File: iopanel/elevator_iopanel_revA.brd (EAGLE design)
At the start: 133.1 x 99.1 mm, 48 parts, among them U2 TLC6C598-Q1, U3 TLC6C598-Q1, U4 SN74HC165DR, U6 TLC6C598-Q1, X3 MSTBA2

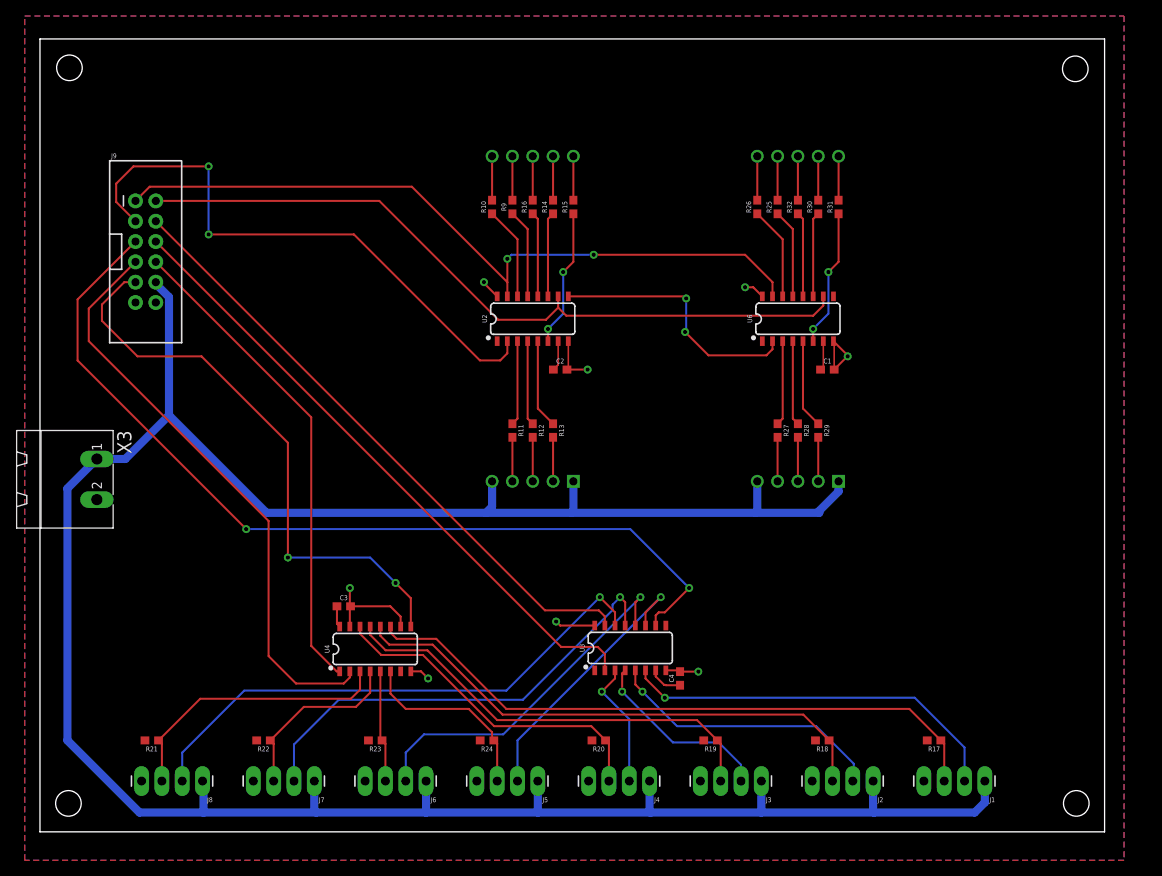
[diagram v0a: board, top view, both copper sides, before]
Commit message: Added LEDs for power rails, silkscreen. sent to fab
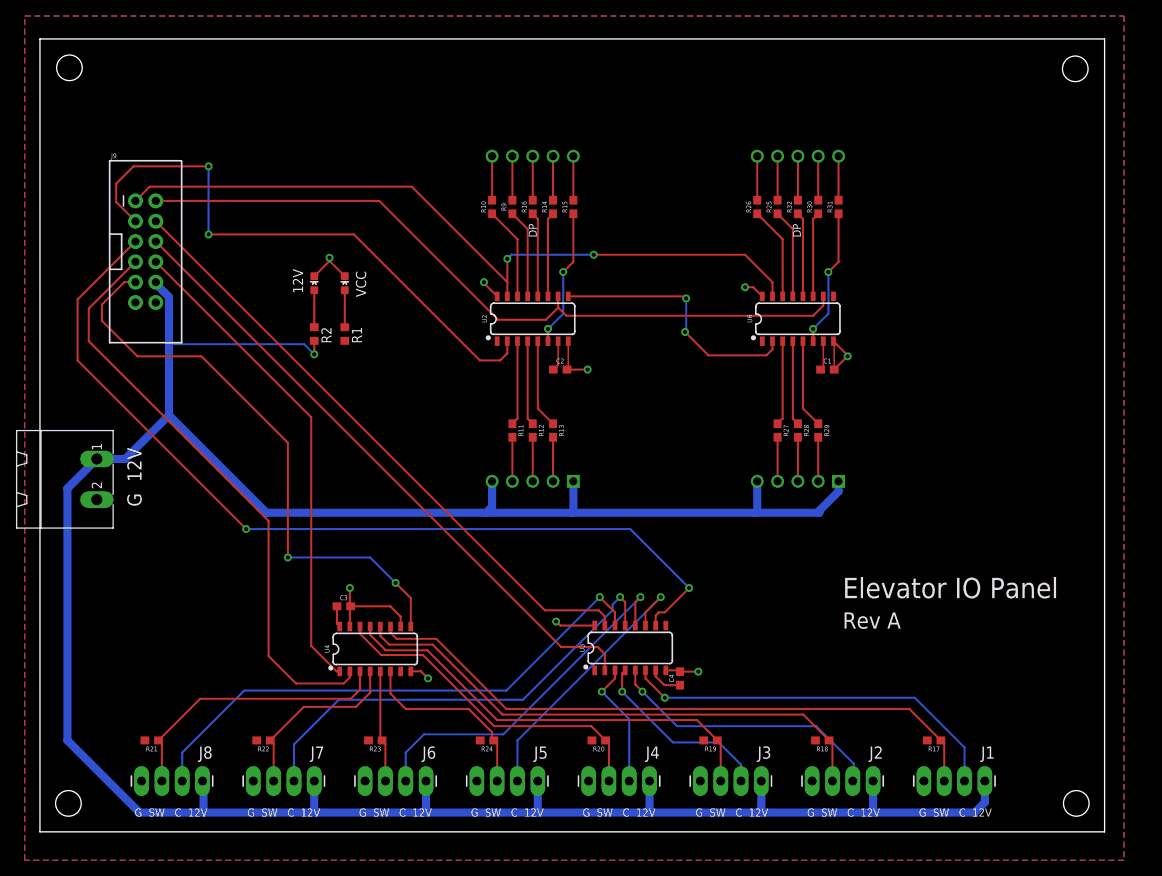
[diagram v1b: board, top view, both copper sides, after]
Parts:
- added LED1, LED2: LED-GREEN0603, BeagleBone_Blue_R3:0603-GREEN
- added R1, R2: (no value), adafruit:R0603
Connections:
- new net N$1: LED1.A, R1.1
- new net N$2: LED2.A, R2.1
- net 12V: now also R2.2
- net GND: now also LED1.C, LED2.C
- net VCC: now also R1.2
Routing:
- net 12V: track 318.4 -> 338.8 mm, vias 0 -> 1
- net GND: track 44.6 -> 50.3 mm, vias 8 -> 9
- net N$2: track 0.00 -> 4.62 mm
- net N$1: track 0.00 -> 4.62 mm
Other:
- board text added: "12V"
- board text added: "DP"
- board text added: "Elevator IO Panel"
- board text added: "G 12V"
- board text added: "G SW C 12V"
- board text added: "Rev A"
- board text added: "VCC"
